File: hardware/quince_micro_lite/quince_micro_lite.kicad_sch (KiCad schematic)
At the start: 46 parts, among them J1 Conn_01x04_Pin, J11 Conn_01x20_Pin, J12 Conn_01x20_Pin, J21 Conn_01x05_Pin, J22 Conn_01x05_Pin, J30 USB_C_Receptacle_USB2.0_14P, J40 Conn_01x10, J50 Micro_SD_Card, U1 CH32V305RBT6, U30 ME6211C33M5, U40 XC6206P-2V8MR, U50 TJA1042TK-3, Y100 12MHz SMD2520

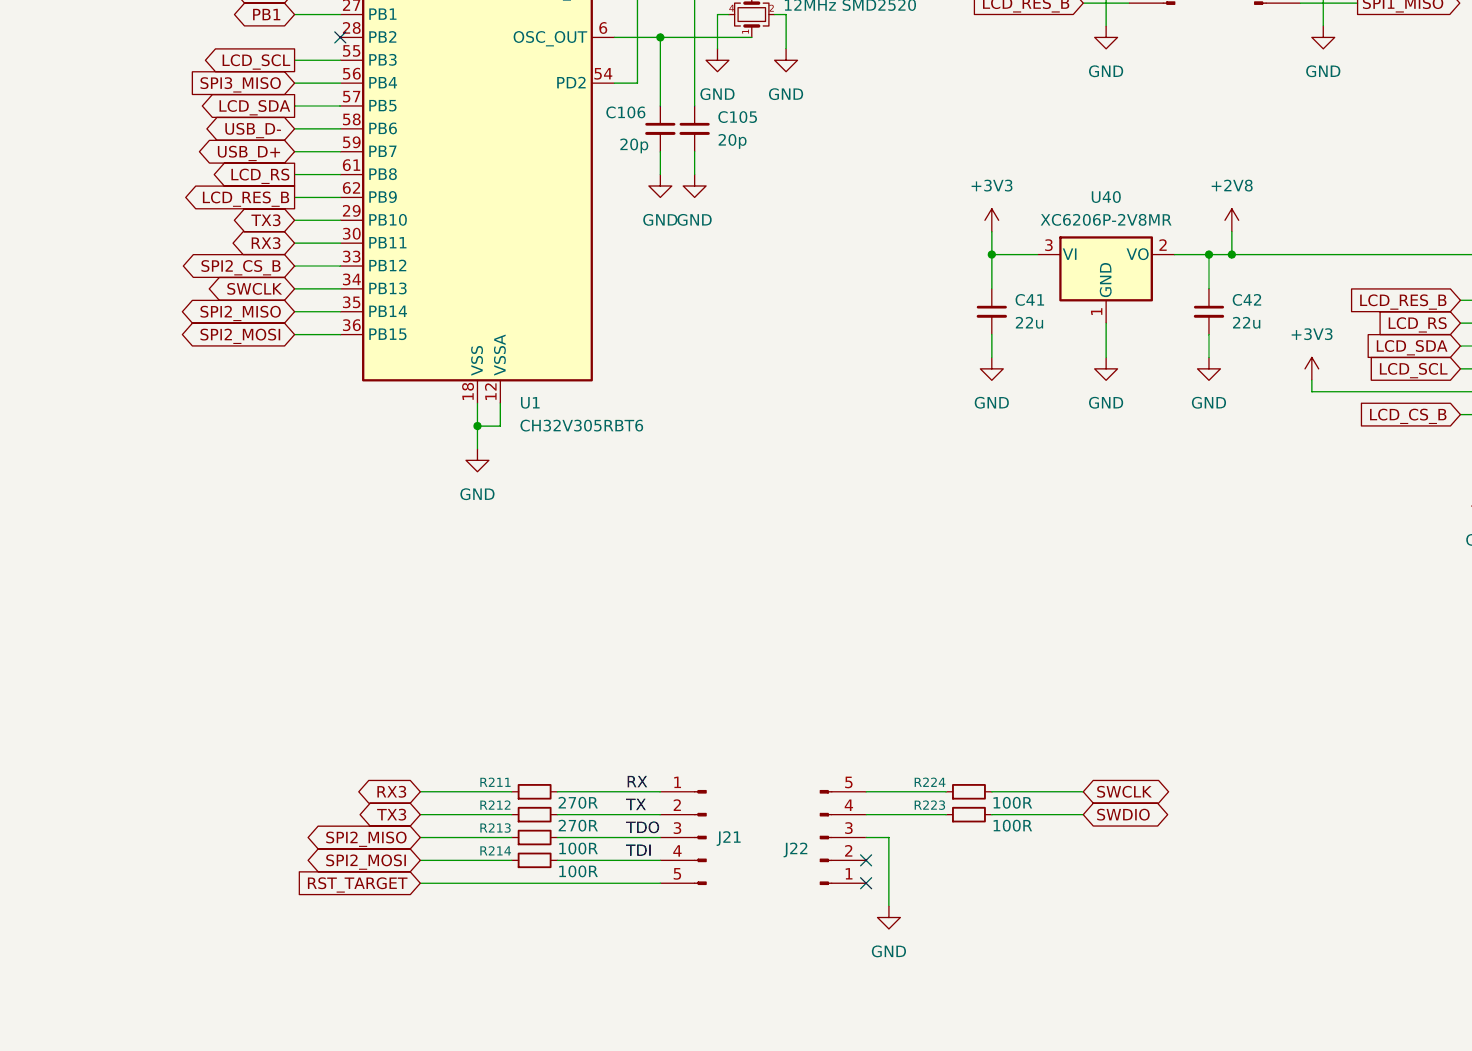
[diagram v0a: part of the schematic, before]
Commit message: version 1.0 commit, changed PB8 and PB9, added 5V and 3.3V supply to debug connector
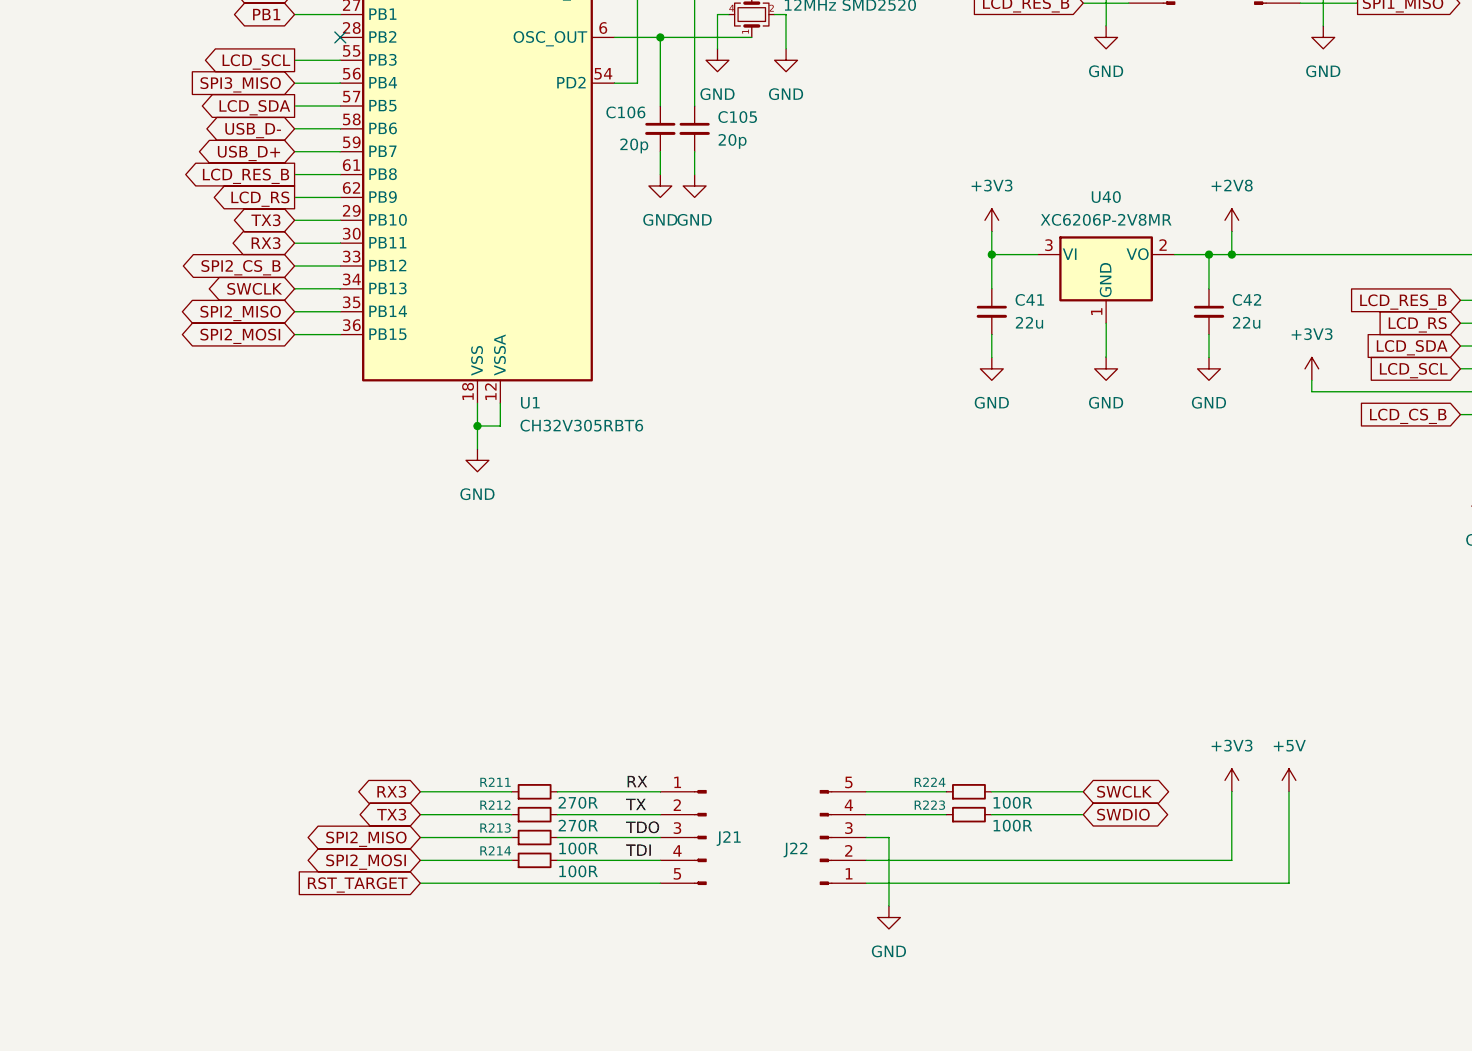
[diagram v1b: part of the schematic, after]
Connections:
- net +3V3: now also J22.2 (Pin_2)
- net +5V: now also J22.1 (Pin_1)
- net LCD_RES_B: now also U1.61 (PB8); no longer U1.62 (PB9)
- net LCD_RS: now also U1.62 (PB9); no longer U1.61 (PB8)
- no-connect marks 19 -> 17
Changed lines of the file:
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@@
 	(title_block
 		(title "Quince micro lite")
-		(date "2025-12-15")
-		(rev "0.9")
+		(date "2026-01-23")
+		(rev "1.0")
 		(company "CyrusDreams")
 		(comment 1 "CERN-OHL-S-2.0")
@@
 	)
 	(no_connect
-		(at 208.28 198.12)
-	)
-	(no_connect
 		(at 180.34 58.42)
 	)
@@
 	)
 	(no_connect
-		(at 208.28 200.66)
-	)
-	(no_connect
 		(at 149.86 53.34)
 	)
@@
 	(wire
 		(pts
+			(xy 255.27 200.66) (xy 208.28 200.66)
+		)
+		(stroke
+			(width 0)
+			(type default)
+		)
+	)
+	(wire
+		(pts
 			(xy 256.54 95.25) (xy 262.89 95.25)
 		)
@@
 	(wire
 		(pts
+			(xy 255.27 190.5) (xy 255.27 200.66)
+		)
+		(stroke
+			(width 0)
+			(type default)
+		)
+	)
+	(wire
+		(pts
 			(xy 133.35 34.29) (xy 133.35 36.83)
 		)
@@
 	(wire
 		(pts
+			(xy 248.92 190.5) (xy 248.92 198.12)
+		)
+		(stroke
+			(width 0)
+			(type default)
+		)
+	)
+	(wire
+		(pts
 			(xy 256.54 59.69) (xy 259.08 59.69)
 		)
@@
 	(wire
 		(pts
+			(xy 248.92 198.12) (xy 208.28 198.12)
+		)
+		(stroke
+			(width 0)
+			(type default)
+		)
+	)
+	(wire
+		(pts
 			(xy 191.77 104.14) (xy 193.04 104.14)
 		)
@@
 	(global_label "LCD_RES_B"
 		(shape output)
-		(at 144.78 124.46 180)
+		(at 144.78 121.92 180)
 		(fields_autoplaced yes)
 		(effects
@@
 		)
 		(property "Intersheetrefs" "${INTERSHEET_REFS}"
-			(at 131.393 124.46 0)
+			(at 131.393 121.92 0)
 			(effects
 				(font
@@
 	(global_label "LCD_RS"
 		(shape output)
-		(at 144.78 121.92 180)
+		(at 144.78 124.46 180)
 		(fields_autoplaced yes)
 		(effects
@@
 		)
 		(property "Intersheetrefs" "${INTERSHEET_REFS}"
-			(at 134.7796 121.92 0)
+			(at 134.7796 124.46 0)
 			(effects
 				(font
@@
 	)
 	(symbol
+		(lib_id "power:+5V")
+		(at 255.27 190.5 0)
+		(unit 1)
+		(exclude_from_sim no)
+		(in_bom yes)
+		(on_board yes)
+		(dnp no)
+		(fields_autoplaced yes)
+		(property "Reference" "#PWR025"
+			(at 255.27 194.31 0)
+			(effects
+				(font
+					(size 1.27 1.27)
+				)
+				(hide yes)
+			)
+		)
+		(property "Value" "+5V"
+			(at 255.27 185.42 0)
+			(effects
+				(font
+					(size 1.27 1.27)
+				)
+			)
+		)
+		(property "Footprint" ""
+			(at 255.27 190.5 0)
+			(effects
+				(font
+					(size 1.27 1.27)
+				)
+				(hide yes)
+			)
+		)
+		(property "Datasheet" ""
+			(at 255.27 190.5 0)
+			(effects
+				(font
+					(size 1.27 1.27)
+				)
+				(hide yes)
+			)
+		)
+		(property "Description" "Power symbol creates a global label with name \"+5V\""
+			(at 255.27 190.5 0)
+			(effects
+				(font
+					(size 1.27 1.27)
+				)
+				(hide yes)
+			)
+		)
+		(pin "1"
+		)
+		(instances
+			(project "quince_micro_lite"
+				(path "/f7b4b346-adb6-4766-81a5-1532c12bdb12"
+					(reference "#PWR025")
+					(unit 1)
+				)
+			)
+		)
+	)
+	(symbol
 		(lib_id "power:GND")
 		(at 276.86 157.48 0)
@@
 					(unit 1)
 				)
+			)
+		)
+	)
+	(symbol
+		(lib_id "power:+3V3")
+		(at 248.92 190.5 0)
+		(unit 1)
+		(exclude_from_sim no)
+		(in_bom yes)
+		(on_board yes)
+		(dnp no)
+		(property "Reference" "#PWR010"
+			(at 248.92 194.31 0)
+			(effects
+				(font
+					(size 1.27 1.27)
+				)
+				(hide yes)
+			)
+		)
+		(property "Value" "+3V3"
+			(at 248.92 185.42 0)
+			(effects
+				(font
+					(size 1.27 1.27)
+				)
+			)
+		)
+		(property "Footprint" ""
+			(at 248.92 190.5 0)
+			(effects
+				(font
+					(size 1.27 1.27)
+				)
+				(hide yes)
+			)
+		)
+		(property "Datasheet" ""
+			(at 248.92 190.5 0)
+			(effects
+				(font
+					(size 1.27 1.27)
+				)
+				(hide yes)
+			)
+		)
+		(property "Description" "Power symbol creates a global label with name \"+3V3\""
+			(at 248.92 190.5 0)
+			(effects
+				(font
+					(size 1.27 1.27)
+				)
+				(hide yes)
+			)
+		)
+		(pin "1"
+		)
+		(instances
+			(project "quince_micro_lite"
+				(path "/f7b4b346-adb6-4766-81a5-1532c12bdb12"
+					(reference "#PWR010")
+					(unit 1)
+				)
